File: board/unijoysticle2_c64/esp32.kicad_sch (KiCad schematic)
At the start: 17 parts, among them Q1 S8050, Q2 S8050, SW1 RESET, SW2 BOOT, U1 ESP32-WROOM-32E

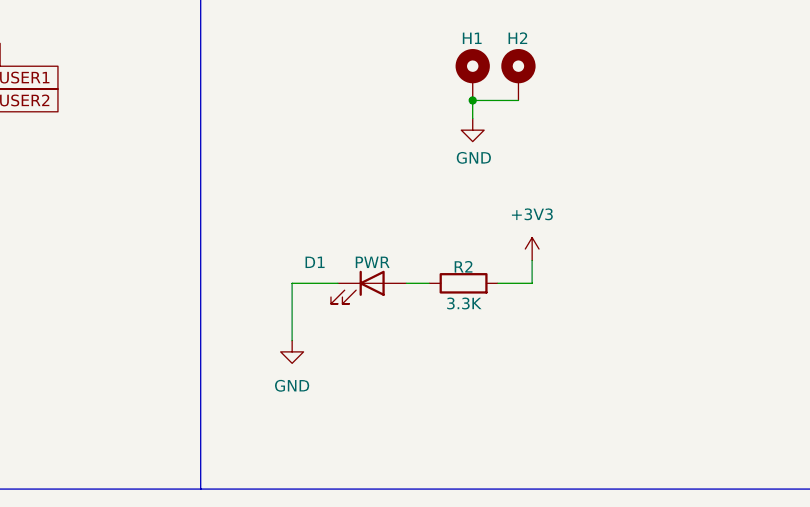
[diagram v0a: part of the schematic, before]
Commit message: c64: more progress on routing
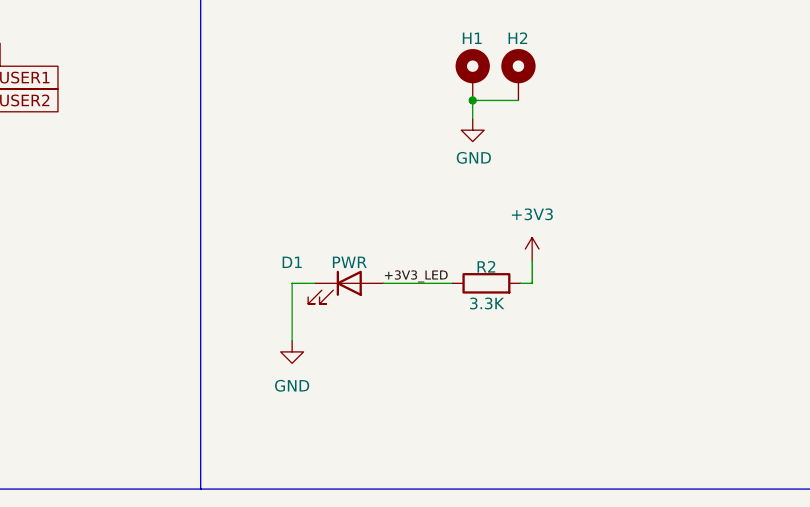
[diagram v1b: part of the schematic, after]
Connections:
- net +3V3_LED: now reaches D1.2 (A), R2.1
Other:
- moved on the sheet: D1, R2
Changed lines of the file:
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@@
     (stroke (width 0) (type default) (color 0 0 0 0))
   )
-  (wire (pts (xy 163.83 130.81) (xy 158.75 130.81))
+  (wire (pts (xy 161.29 130.81) (xy 158.75 130.81))
     (stroke (width 0) (type default) (color 0 0 0 0))
   )
@@
     (stroke (width 0) (type default) (color 0 0 0 0))
   )
-  (wire (pts (xy 181.61 130.81) (xy 185.42 130.81))
+  (wire (pts (xy 184.15 130.81) (xy 185.42 130.81))
     (stroke (width 0) (type default) (color 0 0 0 0))
   )
@@
     (stroke (width 0) (type default) (color 0 0 0 0))
   )
-  (wire (pts (xy 171.45 130.81) (xy 173.99 130.81))
+  (wire (pts (xy 168.91 130.81) (xy 176.53 130.81))
     (stroke (width 0) (type default) (color 0 0 0 0))
   )
@@
   (label "ESP_EN" (at 35.56 86.36 0)
     (effects (font (size 1.27 1.27)) (justify left bottom))
+  )
+  (label "+3V3_LED" (at 168.91 130.81 0)
+    (effects (font (size 1 1)) (justify left bottom))
   )
   (label "ESP_BOOT" (at 111.76 52.07 0)
@@
     (pin "2")
   )
-  (symbol (lib_id "Device:LED") (at 167.64 130.81 0) (unit 1)
-    (in_bom yes) (on_board yes)
-    (property "Reference" "D1" (id 0) (at 161.29 128.524 0))
-    (property "Value" "PWR" (id 1) (at 167.64 128.524 0))
-    (property "Footprint" "LED_SMD:LED_0805_2012Metric_Pad1.15x1.40mm_HandSolder" (id 2) (at 167.64 130.81 0)
-      (effects (font (size 1.27 1.27)) hide)
-    )
-    (property "Datasheet" "~" (id 3) (at 167.64 130.81 0)
-      (effects (font (size 1.27 1.27)) hide)
-    )
-    (property "LCSC" "" (id 4) (at 167.64 130.81 0)
+  (symbol (lib_id "Device:LED") (at 165.1 130.81 0) (unit 1)
+    (in_bom yes) (on_board yes)
+    (property "Reference" "D1" (id 0) (at 158.75 128.524 0))
+    (property "Value" "PWR" (id 1) (at 165.1 128.524 0))
+    (property "Footprint" "LED_SMD:LED_0805_2012Metric_Pad1.15x1.40mm_HandSolder" (id 2) (at 165.1 130.81 0)
+      (effects (font (size 1.27 1.27)) hide)
+    )
+    (property "Datasheet" "~" (id 3) (at 165.1 130.81 0)
+      (effects (font (size 1.27 1.27)) hide)
+    )
+    (property "LCSC" "" (id 4) (at 165.1 130.81 0)
       (effects (font (size 1.27 1.27)) hide)
     )
@@
     (pin "3")
   )
-  (symbol (lib_id "Device:R") (at 177.8 130.81 90) (unit 1)
-    (in_bom yes) (on_board yes)
-    (property "Reference" "R2" (id 0) (at 177.8 129.032 90))
-    (property "Value" "3.3K" (id 1) (at 177.8 133.096 90))
-    (property "Footprint" "Resistor_SMD:R_0805_2012Metric_Pad1.20x1.40mm_HandSolder" (id 2) (at 177.8 132.588 90)
-      (effects (font (size 1.27 1.27)) hide)
-    )
-    (property "Datasheet" "~" (id 3) (at 177.8 130.81 0)
-      (effects (font (size 1.27 1.27)) hide)
-    )
-    (property "LCSC" "" (id 4) (at 177.8 130.81 90)
-      (effects (font (size 1.27 1.27)) hide)
-    )
+  (symbol (lib_id "Device:R") (at 180.34 130.81 90) (unit 1)
+    (in_bom yes) (on_board yes)
+    (property "Reference" "R2" (id 0) (at 180.34 129.032 90))
+    (property "Value" "3.3K" (id 1) (at 180.34 133.096 90))
+    (property "Footprint" "Resistor_SMD:R_0805_2012Metric_Pad1.20x1.40mm_HandSolder" (id 2) (at 180.34 132.588 90)
+      (effects (font (size 1.27 1.27)) hide)
+    )
+    (property "Datasheet" "~" (id 3) (at 180.34 130.81 0)
+      (effects (font (size 1.27 1.27)) hide)
+    )
+    (property "LCSC" "" (id 4) (at 180.34 130.81 90)
+      (effects (font (size 1.27 1.27)) hide)
+    )

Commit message: Unijoysticle C64: Rev C
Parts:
- R2: value 3.3K -> 3K3
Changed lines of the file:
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@@
     (in_bom yes) (on_board yes)
     (property "Reference" "R2" (id 0) (at 180.34 129.032 90))
-    (property "Value" "3.3K" (id 1) (at 180.34 133.096 90))
+    (property "Value" "3K3" (id 1) (at 180.34 133.096 90))
     (property "Footprint" "Resistor_SMD:R_0805_2012Metric_Pad1.20x1.40mm_HandSolder" (id 2) (at 180.34 132.588 90)
       (effects (font (size 1.27 1.27)) hide)
